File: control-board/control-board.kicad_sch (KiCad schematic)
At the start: 90 parts, among them J1 Conn_01x03, J10 DIN-4, J11 DIN-4, J12 Conn_01x03, J13 Conn_01x03, J14 Conn_01x02, J15 Conn_01x03, J2 GPS_ANT, J3 LORA_ANT, J4 DIN-4, J5 DIN-4, J6 USB_C_Receptacle_USB2.0_16P, J7 Conn_01x03, J8 DIN-4, J9 DIN-4, Q1 2N7002, Q2 2N7002, SW1 SW_SPST, U1 STM32H743VITx, U2 NEO-XM, U3 SN65HVD256D, U4 AMS1117-3.3, U6 AMS1117-3.3, U7 SN65HVD256D, Y1 8M, Y2 32.768k

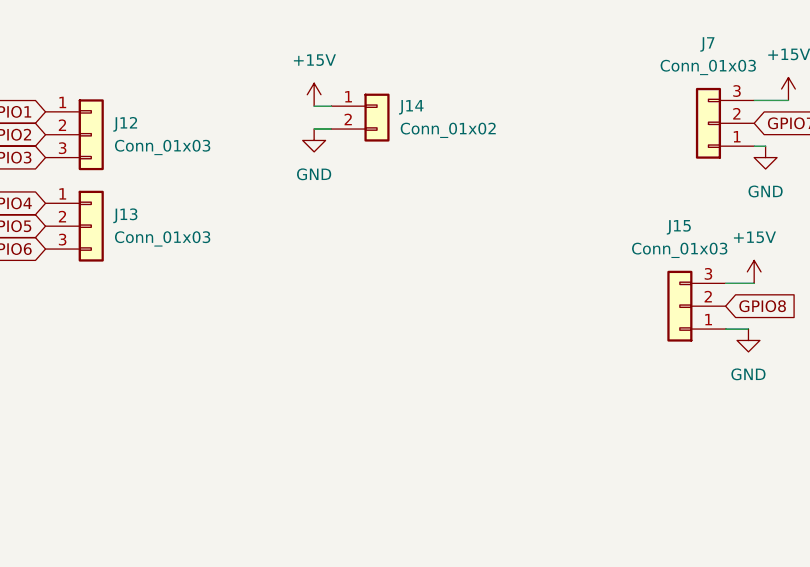
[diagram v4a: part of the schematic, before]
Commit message: modify: add 5V power
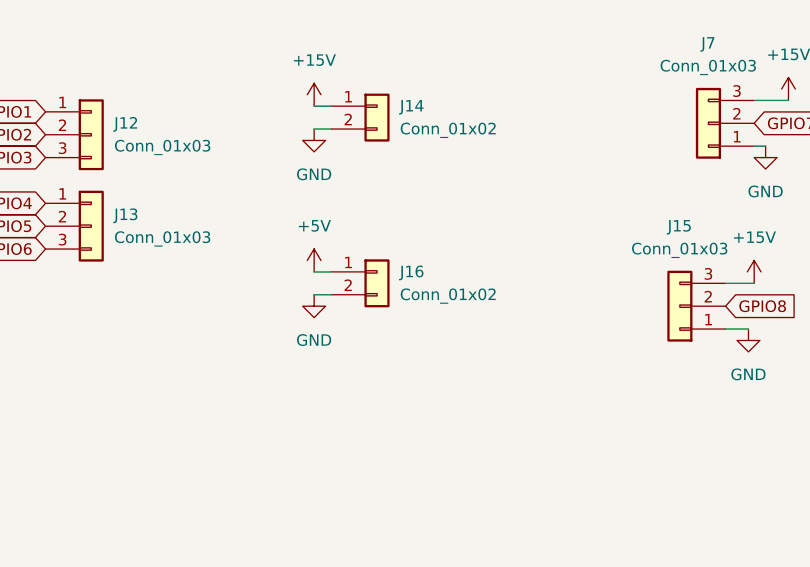
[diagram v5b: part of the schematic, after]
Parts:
- added J16: Conn_01x02, Connector_PinHeader_2.54mm:PinHeader_1x02_P2.54mm_Vertical, symbol Connector_Generic:Conn_01x02
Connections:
- net +5V: now also J16.1 (Pin_1)
- net GND: now also J16.2 (Pin_2)
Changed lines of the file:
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@@
     (stroke (width 0) (type default))
   )
+  (wire (pts (xy 191.77 185.42) (xy 193.675 185.42))
+    (stroke (width 0) (type default))
+  )
   (wire (pts (xy 331.47 168.275) (xy 331.47 167.005))
     (stroke (width 0) (type default))
@@
     (stroke (width 0) (type default))
   )
+  (wire (pts (xy 191.77 187.96) (xy 193.675 187.96))
+    (stroke (width 0) (type default))
+  )
   (wire (pts (xy 57.785 154.305) (xy 59.055 154.305))
     (stroke (width 0) (type default))
@@
     )
   )
+  (symbol (lib_id "Connector_Generic:Conn_01x02") (at 198.755 185.42 0) (unit 1)
+    (in_bom yes) (on_board yes) (dnp no) (fields_autoplaced)
+    (property "Reference" "J16" (at 201.295 185.42 0)
+      (effects (font (size 1.27 1.27)) (justify left))
+    )
+    (property "Value" "Conn_01x02" (at 201.295 187.96 0)
+      (effects (font (size 1.27 1.27)) (justify left))
+    )
+    (property "Footprint" "Connector_PinHeader_2.54mm:PinHeader_1x02_P2.54mm_Vertical" (at 198.755 185.42 0)
+      (effects (font (size 1.27 1.27)) hide)
+    )
+    (property "Datasheet" "~" (at 198.755 185.42 0)
+      (effects (font (size 1.27 1.27)) hide)
+    )
+    (pin "1")
+    (pin "2")
+    (instances
+      (project "control-board"
+        (path "/0d995863-6cec-4b88-9697-48659a6a1176"
+          (reference "J16") (unit 1)
+        )
+      )
+    )
+  )
   (symbol (lib_id "Connector:DIN-4") (at 352.425 140.97 0) (unit 1)
     (in_bom yes) (on_board yes) (dnp no) (fields_autoplaced)
@@
     )
   )
+  (symbol (lib_id "power:+5V") (at 191.77 185.42 0) (unit 1)
+    (in_bom yes) (on_board yes) (dnp no) (fields_autoplaced)
+    (property "Reference" "#PWR088" (at 191.77 189.23 0)
+      (effects (font (size 1.27 1.27)) hide)
+    )
+    (property "Value" "+5V" (at 191.77 180.34 0)
+      (effects (font (size 1.27 1.27)))
+    )
+    (property "Footprint" "" (at 191.77 185.42 0)
+      (effects (font (size 1.27 1.27)) hide)
+    )
+    (property "Datasheet" "" (at 191.77 185.42 0)
+      (effects (font (size 1.27 1.27)) hide)
+    )
+    (pin "1")
+    (instances
+      (project "control-board"
+        (path "/0d995863-6cec-4b88-9697-48659a6a1176"
+          (reference "#PWR088") (unit 1)
+        )
+      )
+    )
+  )
   (symbol (lib_id "Device:C") (at 116.84 191.77 0) (unit 1)
     (in_bom yes) (on_board yes) (dnp no) (fields_autoplaced)
@@
         )
       )
+    )
+  )
+  (symbol (lib_id "power:GND") (at 191.77 187.96 0) (unit 1)
+    (in_bom yes) (on_board yes) (dnp no) (fields_autoplaced)
+    (property "Reference" "#PWR089" (at 191.77 194.31 0)
+      (effects (font (size 1.27 1.27)) hide)
+    )
+    (property "Value" "GND" (at 191.77 193.04 0)
+      (effects (font (size 1.27 1.27)))
+    )
+    (property "Footprint" "" (at 191.77 187.96 0)
+      (effects (font (size 1.27 1.27)) hide)
+    )
+    (property "Datasheet" "" (at 191.77 187.96 0)
+      (effects (font (size 1.27 1.27)) hide)
+    )
+    (pin "1")
+    (instances
+      (project "control-board"
+        (path "/0d995863-6cec-4b88-9697-48659a6a1176"
+          (reference "#PWR089") (unit 1)
+        )
+      )

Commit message: v2025.10
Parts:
- removed Q2: 2N7002, Package_TO_SOT_SMD:SOT-23, symbol Transistor_FET:2N7002
- added D9: LED, LED_SMD:LED_0805_2012Metric, symbol Device:LED
- added J17, J18: Conn_01x02, Connector_PinHeader_2.54mm:PinHeader_1x02_P2.54mm_Vertical, symbol Connector_Generic:Conn_01x02
- added Q2: NXV90EPR, Package_TO_SOT_SMD:SOT-23, symbol Simulation_SPICE:PMOS
- added R8: 10k, Resistor_SMD:R_0603_1608Metric, symbol Device:R_Small
- U3, U7: value SN65HVD256D -> TCAN1462VDRQ1
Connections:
- net +3V3: now also Q2.3 (S); no longer R7.1
- net +5V: now also R8.1
- net CAN1_N: now also J17.1 (Pin_1)
- net CAN1_P: now also J17.2 (Pin_2)
- net CAN2_N: now also J18.1 (Pin_1)
- net CAN2_P: now also J18.2 (Pin_2)
- net GND: now also D7.1 (K), U3.8 (S), U7.8 (S), D9.1 (K)
- net NRST: now reaches R1.2, SW1.2 (B), U1.14 (NRST)
- net NRST: now also Q2.2 (G)
- new net: D9.2 (A), R8.2
- new net: Q2.1 (D), R7.1
- no-connect marks 27 -> 25
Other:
- moved on the sheet: D7, R1, SW1

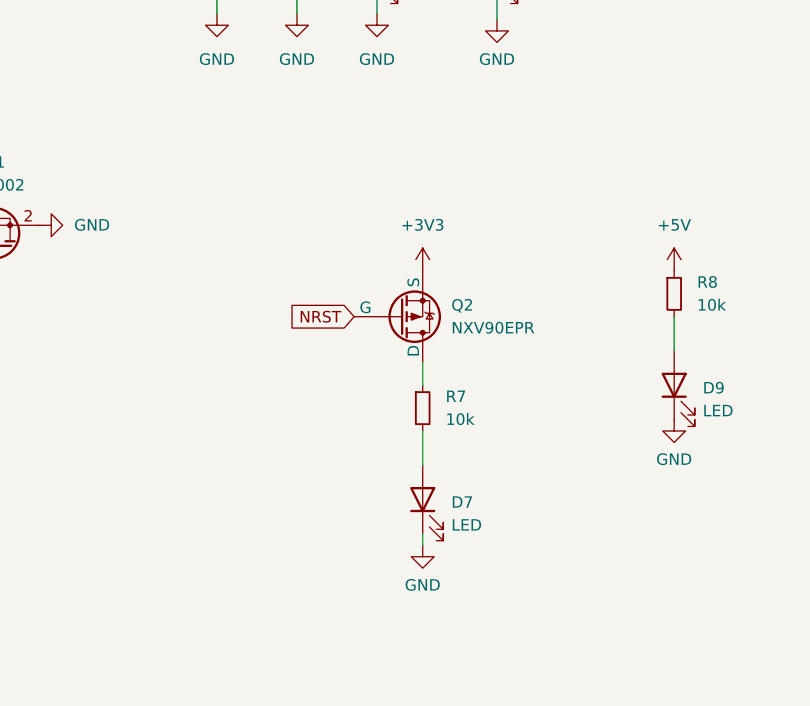
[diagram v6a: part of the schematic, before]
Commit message: fix: SWDIO LED
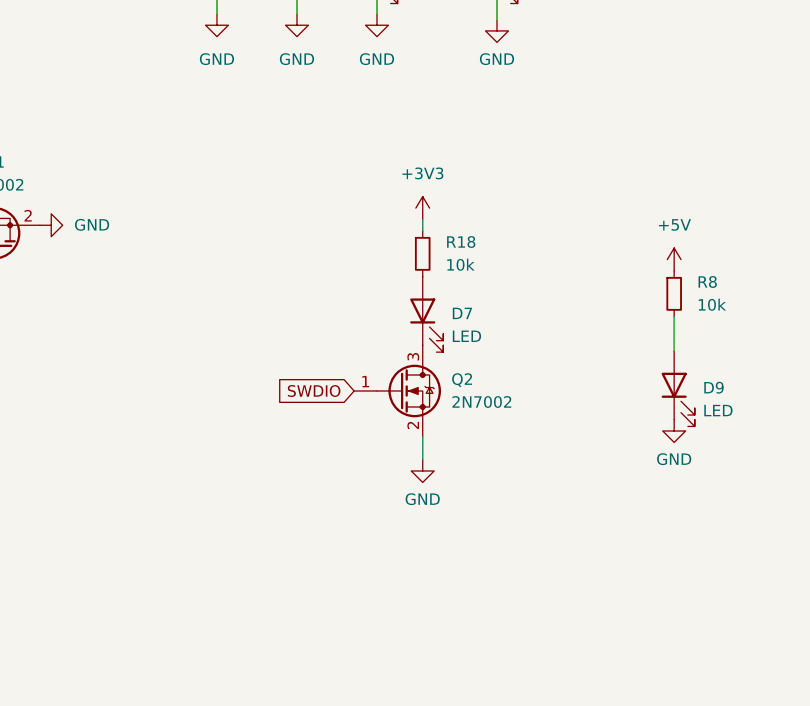
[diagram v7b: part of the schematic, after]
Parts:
- removed Q2: NXV90EPR, Package_TO_SOT_SMD:SOT-23, symbol Simulation_SPICE:PMOS
- removed R7: 10k, Resistor_SMD:R_0603_1608Metric, symbol Device:R_Small
- added Q2: 2N7002, Package_TO_SOT_SMD:SOT-23, symbol Transistor_FET:2N7002
- added R18: 10k, Resistor_SMD:R_0603_1608Metric, symbol Device:R_Small
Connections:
- net +3V3: now also R18.1
- net GND: now also Q2.2 (S); no longer D7.1 (K)
- net SWDIO: now also Q2.1 (G)
- net at D7.2 (A): now also R18.2
- new net: D7.1 (K), Q2.3 (D)
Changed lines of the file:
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@@
   (title_block
     (title "Control Board")
-    (date "2025-10-07")
+    (date "2025-10-10")
     (rev "v2025.10")
     (company "NCKU Formula Racing")
@@
     (stroke (width 0) (type default))
   )
-  (wire (pts (xy 345.44 230.505) (xy 345.44 234.315))
-    (stroke (width 0) (type default))
-  )
   (wire (pts (xy 257.81 137.795) (xy 255.27 137.795))
     (stroke (width 0) (type default))
@@
     (stroke (width 0) (type default))
   )
+  (wire (pts (xy 345.44 207.01) (xy 345.44 208.28))
+    (stroke (width 0) (type default))
+  )
   (wire (pts (xy 79.375 177.165) (xy 81.915 177.165))
     (stroke (width 0) (type default))
@@
     (stroke (width 0) (type default))
   )
-  (wire (pts (xy 345.44 225.425) (xy 345.44 222.885))
+  (wire (pts (xy 345.44 233.68) (xy 345.44 231.14))
     (stroke (width 0) (type default))
   )
@@
     (stroke (width 0) (type default))
   )
-  (wire (pts (xy 345.44 241.935) (xy 345.44 243.205))
-    (stroke (width 0) (type default))
-  )
   (wire (pts (xy 93.98 195.58) (xy 93.98 198.12))
     (stroke (width 0) (type default))
@@
     )
   )
-  (global_label "NRST" (shape input) (at 337.82 217.805 180) (fields_autoplaced)
-    (effects (font (size 1.27 1.27)) (justify right))
-    (property "Intersheetrefs" "${INTERSHEET_REFS}" (at 330.0572 217.805 0)
-      (effects (font (size 1.27 1.27)) (justify right) hide)
-    )
-  )
   (global_label "CAN1_N" (shape input) (at 133.985 104.775 0) (fields_autoplaced)
     (effects (font (size 1.27 1.27)) (justify left))
@@
     )
   )
+  (global_label "SWDIO" (shape input) (at 337.82 226.06 180) (fields_autoplaced)
+    (effects (font (size 1.27 1.27)) (justify right))
+    (property "Intersheetrefs" "${INTERSHEET_REFS}" (at 328.9686 226.06 0)
+      (effects (font (size 1.27 1.27)) (justify right) hide)
+    )
+  )
   (symbol (lib_id "Device:C") (at 139.7 191.77 0) (unit 1)
     (in_bom yes) (on_board yes) (dnp no) (fields_autoplaced)
@@
     )
   )
-  (symbol (lib_id "Device:LED") (at 345.44 238.125 90) (unit 1)
-    (in_bom yes) (on_board yes) (dnp no) (fields_autoplaced)
-    (property "Reference" "D7" (at 348.615 238.4425 90)
-      (effects (font (size 1.27 1.27)) (justify right))
-    )
-    (property "Value" "LED" (at 348.615 240.9825 90)
-      (effects (font (size 1.27 1.27)) (justify right))
-    )
-    (property "Footprint" "LED_SMD:LED_0805_2012Metric" (at 345.44 238.125 0)
-      (effects (font (size 1.27 1.27)) hide)
-    )
-    (property "Datasheet" "~" (at 345.44 238.125 0)
-      (effects (font (size 1.27 1.27)) hide)
-    )
-    (pin "1")
-    (pin "2")
-    (instances
-      (project "control-board"
-        (path "/0d995863-6cec-4b88-9697-48659a6a1176"
-          (reference "D7") (unit 1)
-        )
-      )
-    )
-  )
   (symbol (lib_id "Connector_Generic:Conn_01x02") (at 198.755 185.42 0) (unit 1)
     (in_bom yes) (on_board yes) (dnp no) (fields_autoplaced)
@@
     )
   )
-  (symbol (lib_id "power:GND") (at 345.44 243.205 0) (unit 1)
+  (symbol (lib_id "power:GND") (at 345.44 233.68 0) (unit 1)
     (in_bom yes) (on_board yes) (dnp no) (fields_autoplaced)
-    (property "Reference" "#PWR030" (at 345.44 249.555 0)
+    (property "Reference" "#PWR030" (at 345.44 240.03 0)
       (effects (font (size 1.27 1.27)) hide)
     )
-    (property "Value" "GND" (at 345.44 247.65 0)
+    (property "Value" "GND" (at 345.44 238.125 0)
       (effects (font (size 1.27 1.27)))
     )
-    (property "Footprint" "" (at 345.44 243.205 0)
+    (property "Footprint" "" (at 345.44 233.68 0)
       (effects (font (size 1.27 1.27)) hide)
     )
-    (property "Datasheet" "" (at 345.44 243.205 0)
+    (property "Datasheet" "" (at 345.44 233.68 0)
       (effects (font (size 1.27 1.27)) hide)
     )
@@
     )
   )
-  (symbol (lib_id "power:+3V3") (at 345.44 212.725 0) (unit 1)
+  (symbol (lib_id "power:+3V3") (at 345.44 207.01 0) (unit 1)
     (in_bom yes) (on_board yes) (dnp no) (fields_autoplaced)
-    (property "Reference" "#PWR093" (at 345.44 216.535 0)
+    (property "Reference" "#PWR093" (at 345.44 210.82 0)
       (effects (font (size 1.27 1.27)) hide)
     )
-    (property "Value" "+3V3" (at 345.44 207.645 0)
+    (property "Value" "+3V3" (at 345.44 201.93 0)
       (effects (font (size 1.27 1.27)))
     )
-    (property "Footprint" "" (at 345.44 212.725 0)
+    (property "Footprint" "" (at 345.44 207.01 0)
       (effects (font (size 1.27 1.27)) hide)
     )
-    (property "Datasheet" "" (at 345.44 212.725 0)
+    (property "Datasheet" "" (at 345.44 207.01 0)
       (effects (font (size 1.27 1.27)) hide)
     )
@@
     )
   )
-  (symbol (lib_id "Device:R_Small") (at 345.44 227.965 0) (unit 1)
-    (in_bom yes) (on_board yes) (dnp no) (fields_autoplaced)
-    (property "Reference" "R7" (at 347.98 226.695 0)
-      (effects (font (size 1.27 1.27)) (justify left))
-    )
-    (property "Value" "10k" (at 347.98 229.235 0)
-      (effects (font (size 1.27 1.27)) (justify left))
-    )
-    (property "Footprint" "Resistor_SMD:R_0603_1608Metric" (at 345.44 227.965 0)
-      (effects (font (size 1.27 1.27)) hide)
-    )
-    (property "Datasheet" "~" (at 345.44 227.965 0)
-      (effects (font (size 1.27 1.27)) hide)
-    )
-    (pin "1")
-    (pin "2")
-    (instances
-      (project "control-board"
-        (path "/0d995863-6cec-4b88-9697-48659a6a1176"
-          (reference "R7") (unit 1)
-        )
-      )
-    )
-  )
   (symbol (lib_id "Connector:DIN-4") (at 385.445 106.045 0) (unit 1)
     (in_bom yes) (on_board yes) (dnp no) (fields_autoplaced)
@@
     )
   )
-  (symbol (lib_id "Simulation_SPICE:PMOS") (at 342.9 217.805 0) (mirror x) (unit 1)
-    (in_bom yes) (on_board yes) (dnp no)
-    (property "Reference" "Q2" (at 348.615 216.535 0)
-      (effects (font (size 1.27 1.27)) (justify left))
-    )
-    (property "Value" "NXV90EPR" (at 348.615 219.075 0)
-      (effects (font (size 1.27 1.27)) (justify left))
-    )
-    (property "Footprint" "Package_TO_SOT_SMD:SOT-23" (at 347.98 220.345 0)
-      (effects (font (size 1.27 1.27)) hide)
-    )
-    (property "Datasheet" "https://ngspice.sourceforge.io/docs/ngspice-manual.pdf" (at 342.9 205.105 0)
-      (effects (font (size 1.27 1.27)) hide)
-    )
-    (property "Sim.Device" "PMOS" (at 342.9 200.66 0)
-      (effects (font (size 1.27 1.27)) hide)
-    )
-    (property "Sim.Type" "VDMOS" (at 342.9 198.755 0)
-      (effects (font (size 1.27 1.27)) hide)
-    )
-    (property "Sim.Pins" "1=D 2=G 3=S" (at 342.9 202.565 0)
-      (effects (font (size 1.27 1.27)) hide)
-    )
-    (pin "2")
-    (pin "3")
-    (pin "1")
-    (instances
-      (project "control-board"
-        (path "/0d995863-6cec-4b88-9697-48659a6a1176"
-          (reference "Q2") (unit 1)
-        )
-      )
-    )
-  )
   (symbol (lib_id "Mechanical:MountingHole_Pad") (at 78.105 226.695 90) (unit 1)
     (in_bom yes) (on_board yes) (dnp no) (fields_autoplaced)
@@
     )
   )
+  (symbol (lib_id "Device:R_Small") (at 345.44 210.82 0) (unit 1)
+    (in_bom yes) (on_board yes) (dnp no) (fields_autoplaced)
+    (property "Reference" "R18" (at 347.98 209.55 0)
+      (effects (font (size 1.27 1.27)) (justify left))
+    )
+    (property "Value" "10k" (at 347.98 212.09 0)
+      (effects (font (size 1.27 1.27)) (justify left))
+    )
+    (property "Footprint" "Resistor_SMD:R_0603_1608Metric" (at 345.44 210.82 0)
+      (effects (font (size 1.27 1.27)) hide)
+    )
+    (property "Datasheet" "~" (at 345.44 210.82 0)
+      (effects (font (size 1.27 1.27)) hide)
+    )
+    (pin "1")
+    (pin "2")
+    (instances
+      (project "control-board"
+        (path "/0d995863-6cec-4b88-9697-48659a6a1176"
+          (reference "R18") (unit 1)
+        )
+      )
+    )
+  )
   (symbol (lib_id "Regulator_Linear:AMS1117-3.3") (at 198.755 137.795 0) (unit 1)
     (in_bom yes) (on_board yes) (dnp no) (fields_autoplaced)
@@
     )
   )
+  (symbol (lib_id "Device:LED") (at 345.44 217.17 90) (unit 1)
+    (in_bom yes) (on_board yes) (dnp no) (fields_autoplaced)
+    (property "Reference" "D7" (at 348.615 217.4875 90)
+      (effects (font (size 1.27 1.27)) (justify right))
+    )
+    (property "Value" "LED" (at 348.615 220.0275 90)
+      (effects (font (size 1.27 1.27)) (justify right))
+    )
+    (property "Footprint" "LED_SMD:LED_0805_2012Metric" (at 345.44 217.17 0)
+      (effects (font (size 1.27 1.27)) hide)
+    )
+    (property "Datasheet" "~" (at 345.44 217.17 0)
+      (effects (font (size 1.27 1.27)) hide)
+    )
+    (pin "1")
+    (pin "2")
+    (instances
+      (project "control-board"
+        (path "/0d995863-6cec-4b88-9697-48659a6a1176"
+          (reference "D7") (unit 1)
+        )
+      )
+    )
+  )
   (symbol (lib_id "power:+5V") (at 295.275 112.395 0) (unit 1)
     (in_bom yes) (on_board yes) (dnp no) (fields_autoplaced)
@@
         )
       )
+    )
+  )
+  (symbol (lib_id "Transistor_FET:2N7002") (at 342.9 226.06 0) (unit 1)
+    (in_bom yes) (on_board yes) (dnp no) (fields_autoplaced)
+    (property "Reference" "Q2" (at 348.615 224.79 0)
+      (effects (font (size 1.27 1.27)) (justify left))
+    )
+    (property "Value" "2N7002" (at 348.615 227.33 0)
+      (effects (font (size 1.27 1.27)) (justify left))
+    )
+    (property "Footprint" "Package_TO_SOT_SMD:SOT-23" (at 347.98 227.965 0)
+      (effects (font (size 1.27 1.27) italic) (justify left) hide)
+    )
+    (property "Datasheet" "https://www.onsemi.com/pub/Collateral/NDS7002A-D.PDF" (at 347.98 229.87 0)
+      (effects (font (size 1.27 1.27)) (justify left) hide)
+    )
+    (pin "1")
+    (pin "2")
+    (pin "3")
+    (instances
+      (project "control-board"
+        (path "/0d995863-6cec-4b88-9697-48659a6a1176"
+          (reference "Q2") (unit 1)
+        )
+      )
